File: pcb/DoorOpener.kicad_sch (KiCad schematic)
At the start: 19 parts, among them J1 Serial, J2 Serial, J3 14V, SW1 POWER, SW2 Button, SW4 Button, SW5 Reset, U1 ESP-01v090, U2 ESP-01v090, U3 dcdc, U4 relais_module

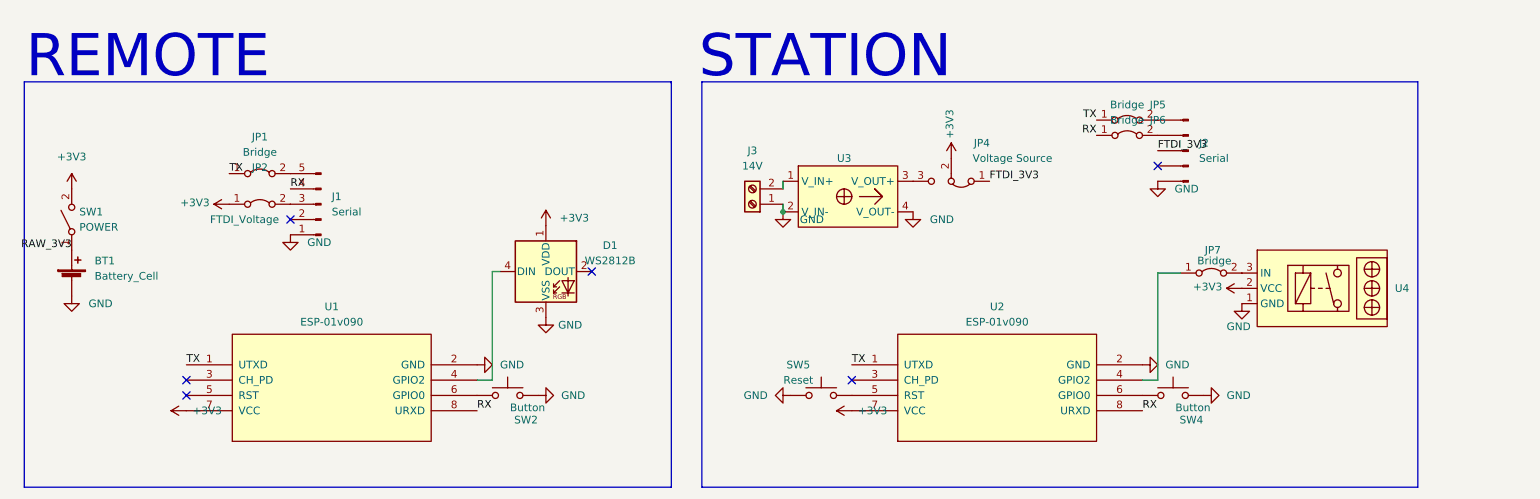
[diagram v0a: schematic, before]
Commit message: Fix wrong polarity of the dcdc module and replace the relais circuit
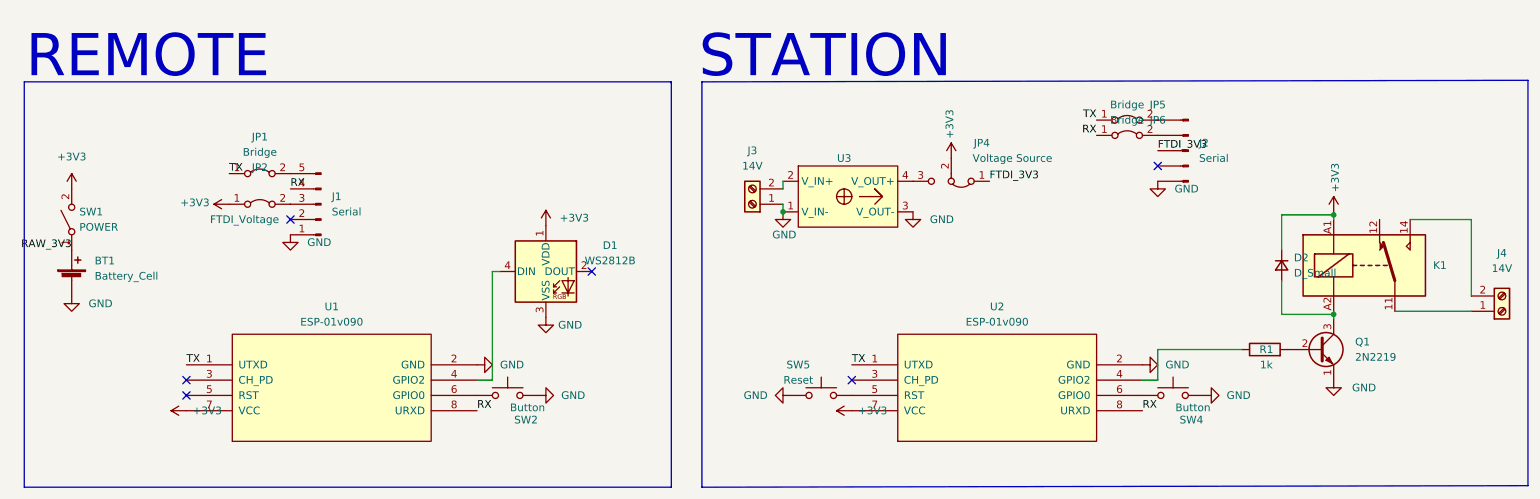
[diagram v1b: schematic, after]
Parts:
- removed JP7: Bridge, Resistor_THT:R_Axial_DIN0204_L3.6mm_D1.6mm_P5.08mm_Horizontal, symbol Jumper:Jumper_2_Bridged
- removed U4: relais_module, relais_module:relais_module, symbol relais_module:relais_module
- added D2: D_Small, Diode_THT:D_A-405_P7.62mm_Horizontal, symbol Device:D_Small
- added J4: 14V, TerminalBlock_Phoenix:TerminalBlock_Phoenix_PT-1,5-2-3.5-H_1x02_P3.50mm_Horizontal, symbol Connector:Screw_Terminal_01x02
- added K1: FINDER-36.11, Relay_THT:Relay_SPDT_Finder_36.11, symbol Relay:FINDER-36.11
- added Q1: 2N2219, Connector_PinHeader_2.54mm:PinHeader_1x03_P2.54mm_Vertical, symbol Transistor_BJT:2N2219
- added R1: 1k, Resistor_THT:R_Axial_DIN0204_L3.6mm_D1.6mm_P7.62mm_Horizontal, symbol Device:R
- JP5: footprint Resistor_THT:R_Axial_DIN0204_L3.6mm_D1.6mm_P5.08mm_Horizontal -> Resistor_THT:R_Axial_DIN0204_L3.6mm_D1.6mm_P7.62mm_Horizontal
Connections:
- net +3V3: now also D2.1 (K), K1.A1
- net GND: now also U3.1 (V_IN-), U3.3 (V_OUT-), Q1.1 (E); no longer U3.2 (V_IN-), U3.4 (V_OUT-)
- net at U2.4 (GPIO2): now also R1.1
- net at J3.2 (Pin_2): now also U3.2 (V_IN+); no longer U3.1 (V_IN+)
- net at JP4.3 (B): now also U3.4 (V_OUT+); no longer U3.3 (V_OUT+)
- new net: J4.1 (Pin_1), K1.11
- new net: J4.2 (Pin_2), K1.14
- new net: D2.2 (A), K1.A2, Q1.3 (C)
- new net: Q1.2 (B), R1.2

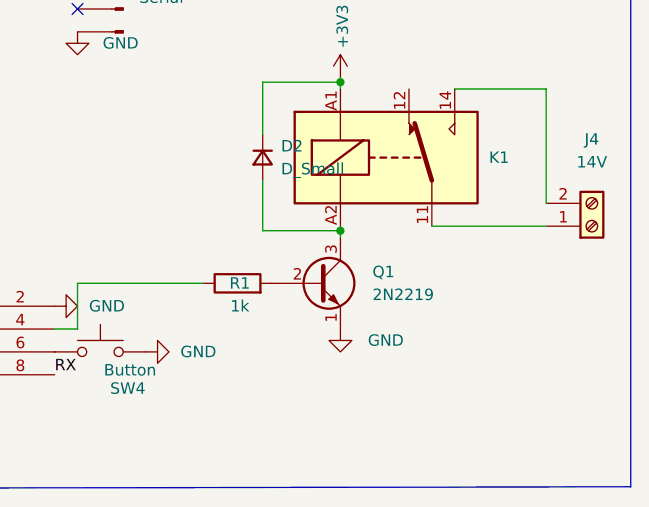
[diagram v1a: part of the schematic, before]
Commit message: Label the transistor
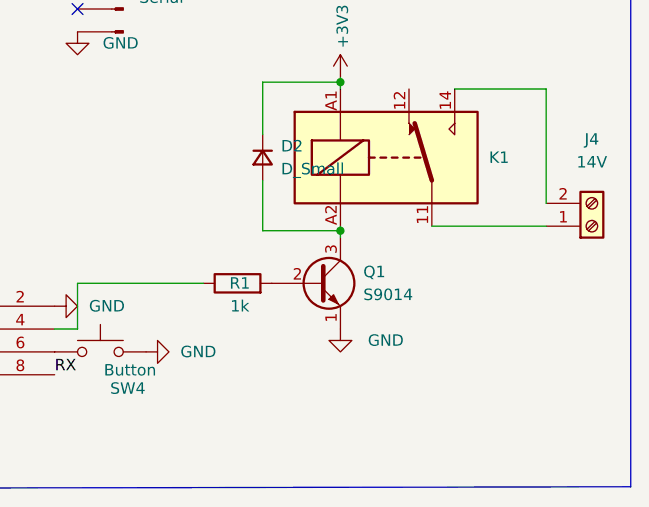
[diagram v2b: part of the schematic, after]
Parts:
- Q1: value 2N2219 -> S9014
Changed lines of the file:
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@@
   (symbol (lib_id "Transistor_BJT:2N2219") (at 251.46 88.9 0) (unit 1)
     (in_bom yes) (on_board yes) (fields_autoplaced)
-    (property "Reference" "Q1" (id 0) (at 257.556 87.6299 0)
-      (effects (font (size 1.27 1.27)) (justify left))
-    )
-    (property "Value" "2N2219" (id 1) (at 257.556 90.1699 0)
+    (property "Reference" "Q1" (id 0) (at 256.54 87.6299 0)
+      (effects (font (size 1.27 1.27)) (justify left))
+    )
+    (property "Value" "S9014" (id 1) (at 256.54 90.1699 0)
       (effects (font (size 1.27 1.27)) (justify left))
     )
@@
     )
     (path "/cf0b7d27-a11d-435d-98da-8ba0494133c3"
-      (reference "Q1") (unit 1) (value "2N2219") (footprint "Connector_PinHeader_2.54mm:PinHeader_1x03_P2.54mm_Vertical")
+      (reference "Q1") (unit 1) (value "S9014") (footprint "Connector_PinHeader_2.54mm:PinHeader_1x03_P2.54mm_Vertical")
     )
     (path "/7f18b4db-7605-48d5-b647-dc87e52d5224"

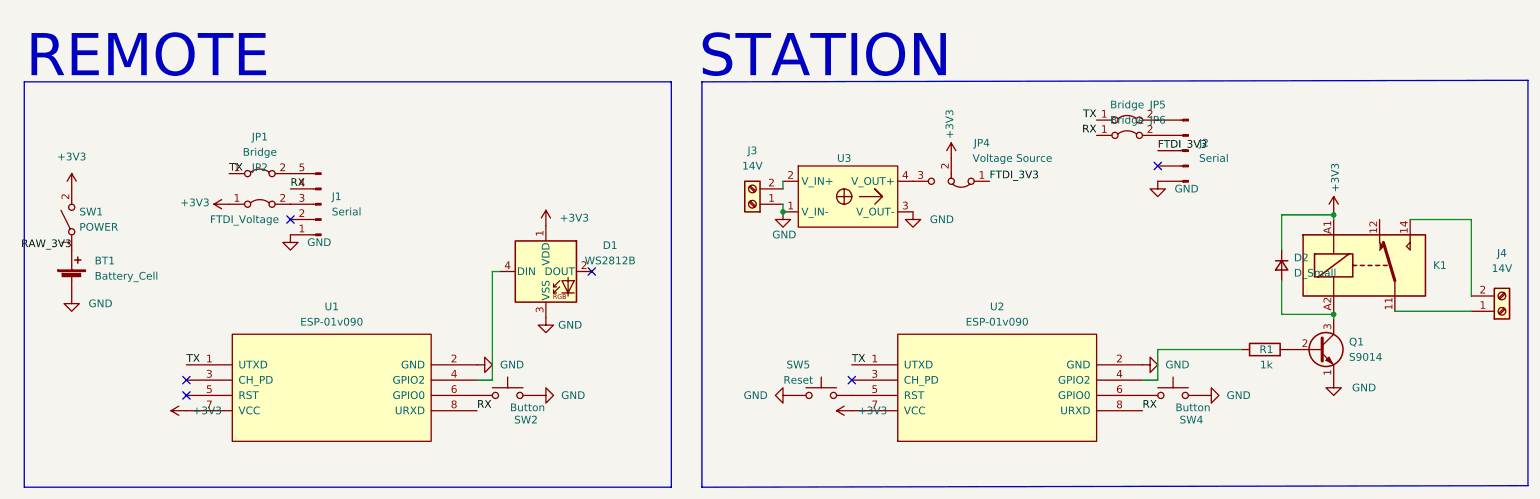
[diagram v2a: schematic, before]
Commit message: Add polarised capacitors for improved stability
Also add  a three way switch for the remote so that the jumper does not get lost and to decouple the battery when FTDI is used.
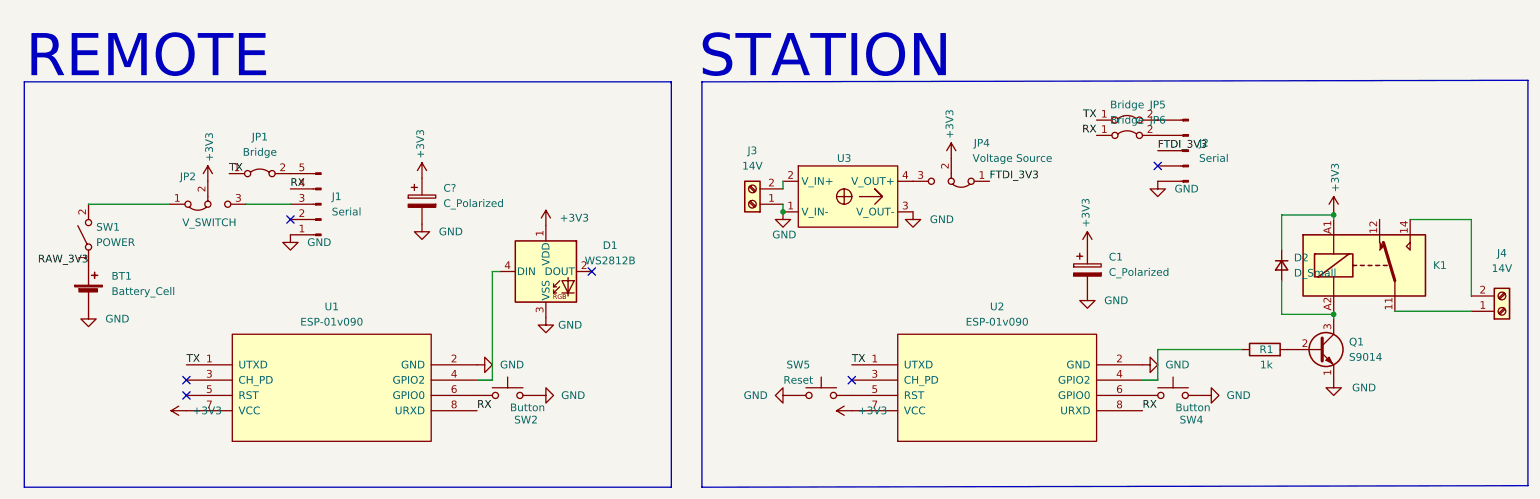
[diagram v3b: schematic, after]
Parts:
- added C1, C?: C_Polarized, Capacitor_THT:CP_Radial_D5.0mm_P2.50mm, symbol Device:C_Polarized
- JP2: value FTDI_Voltage -> V_SWITCH; footprint Connector_PinHeader_2.54mm:PinHeader_1x02_P2.54mm_Vertical -> Connector_PinHeader_2.54mm:PinHeader_1x03_P2.54mm_Vertical; symbol Jumper:Jumper_2_Bridged -> Jumper:Jumper_3_Bridged12
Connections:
- net +3V3: now also JP2.2 (C), C1.1, C?.1; no longer JP2.1 (A), SW1.2 (B)
- net GND: now also C1.2, C?.2
- net at J1.3 (Pin_3): now also JP2.3 (B); no longer JP2.2 (B)
- new net: JP2.1 (A), SW1.2 (B)
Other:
- moved on the sheet: BT1, SW1
